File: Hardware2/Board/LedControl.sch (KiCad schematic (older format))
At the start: 49 parts, among them J2 Jumper, J3 Jumper, P1 USB_OTG, P10 TP, P11 2059-302, P12 DISPLAY, P13 TP, P14 Conn_01x03, P15 TP, P16 2059-302, P17 2059-302, P18 CONN_01X03, P19 CONN_01X03, P2 TP, P3 TP, P32 TP, P33 TP, P34 TP, P4 TP, P5 2059-302, P6 TP, P7 TP, P8 Micro_SD, P9 TP, SW1 PEC12R-4215F-S0024, SW2 PEC12R-4215F-S0024, U1 STM32L433CCUx, U2 SP485CN, U3 SP485CN, U4 SP485CN, X1 IQXO/7X

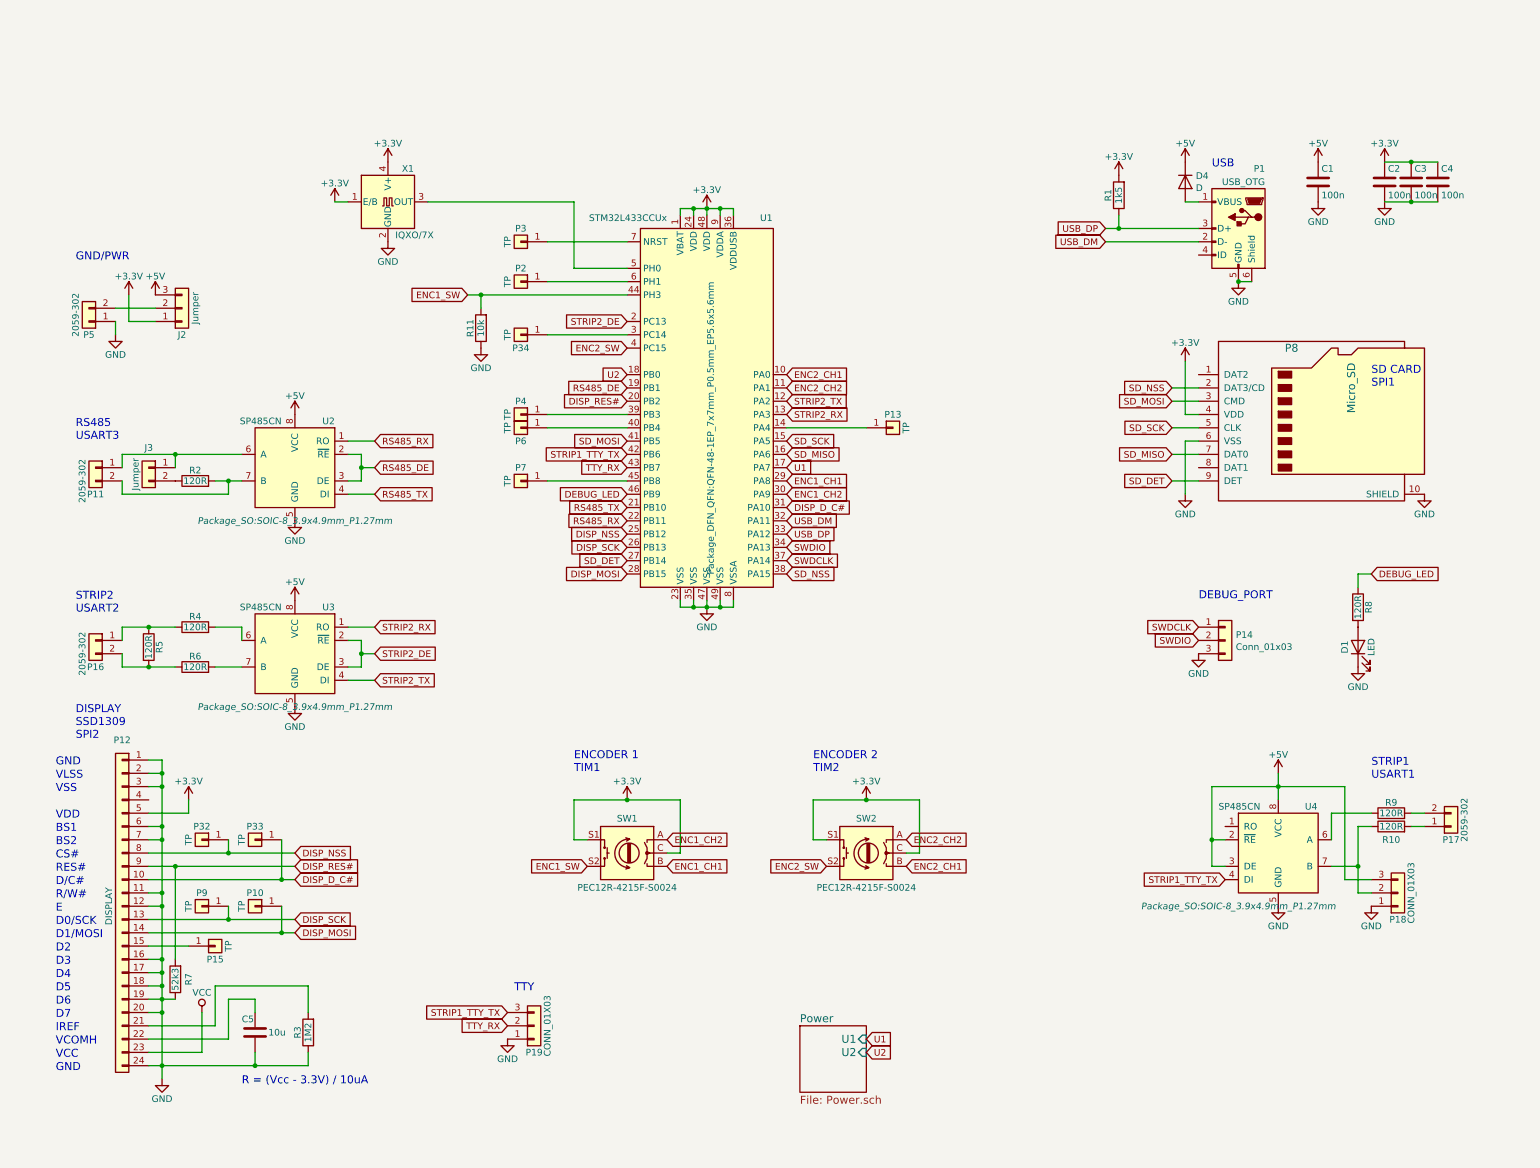
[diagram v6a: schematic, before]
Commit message: LED strip power supply below strip
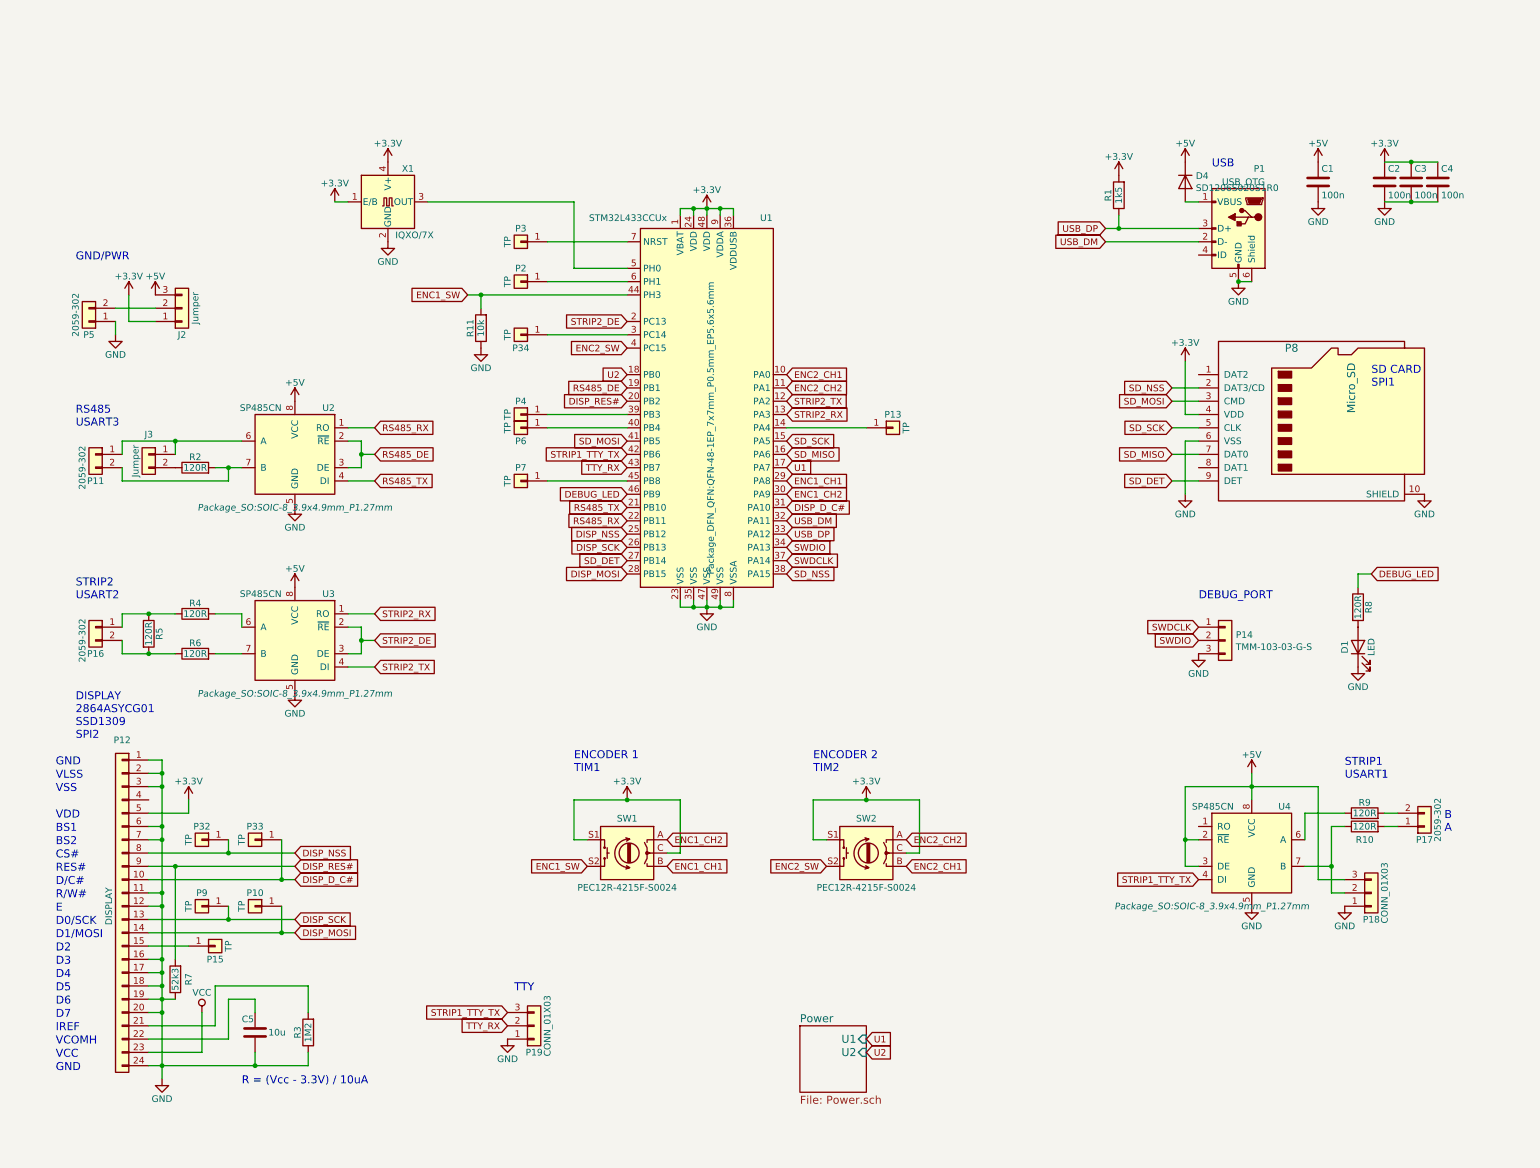
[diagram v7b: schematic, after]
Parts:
- D4: value D -> SD1206S020S1R0
- P14: value Conn_01x03 -> TMM-103-03-G-S
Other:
- note added: "B\nA"
- note added: "DISPLAY\n2864ASYCG01\nSSD1309\nSPI2"
- note removed: "DISPLAY\nSSD1309\nSPI2"
- moved on the sheet: J3, P11, P16, P17, P18, R10, R2, R4, R5, R6, R9, U2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

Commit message: Add CAN bus
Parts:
- removed J3: Jumper, LedControl:Jumper, symbol Connector_Generic:Conn_01x02
- removed P19: CONN_01X03, Connector_PinHeader_2.54mm:PinHeader_1x03_P2.54mm_Vertical, symbol Connector_Generic:Conn_01x03
- removed P3: TP, LedControl:Pad, symbol Connector_Generic:Conn_01x01
- removed U3: SP485CN, Package_SO:SOIC-8_3.9x4.9mm_P1.27mm, symbol Interface_UART:SP3485CN
- added C15, C16, C17: 100n, Capacitor_SMD:C_0603_1608Metric, symbol Device:C
- added D5, D6: SD1206S020S1R0, Diode_SMD:D_1206_3216Metric, symbol Device:D
- added J2: Jumper, LedControl:Jumper, symbol Connector_Generic:Conn_01x02
- added J3, J5: Jumper, LedControl:Jumper3, symbol Connector_Generic:Conn_01x04
- added P11: Header, Connector_PinHeader_2.54mm:PinHeader_1x04_P2.54mm_Vertical, symbol Connector_Generic:Conn_01x04
- added P17, P2, P4, P6, P9: 2059-302, LedControl:WAGO_2059-302, symbol Connector_Generic:Conn_01x02
- added P41, P42, P43, P44: TP, LedControl:Pad, symbol Connector_Generic:Conn_01x01
- added Q1, Q2: DMG1012UW, Package_TO_SOT_SMD:SOT-323_SC-70, symbol Transistor_FET:BSS214NW
- added R23, R24, R26, R28: 120R, Resistor_SMD:R_1206_3216Metric, symbol Device:R
- added R25, R27, R29, R8: 10k, Resistor_SMD:R_0603_1608Metric, symbol Device:R
- added U10: SP485CN, Package_SO:SOIC-8_3.9x4.9mm_P1.27mm, symbol Interface_UART:SP3485CN
- added U2: SN65HVD230, Package_SO:SOIC-8_3.9x4.9mm_P1.27mm, symbol Interface_CAN_LIN:SN65HVD230
- J4: renamed from J2; symbol Connector_Generic:Conn_01x03 -> Connector_Generic:Conn_01x04
- R22: renamed from R8; value 120R -> 390R; footprint Resistor_SMD:R_1206_3216Metric -> Resistor_SMD:R_0603_1608Metric
- R4, R6: value 120R -> 390R; footprint Resistor_SMD:R_1206_3216Metric -> Resistor_SMD:R_0603_1608Metric
- renumbered P8 to P10, P2 to P16, P7 to P19, P16 to P3, P4 to P36, P9 to P38, P6 to P39, P10 to P40, P11 to P7, P17 to P8, U2 to U3
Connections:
- net STRIP2_DE is gone; now on an unnamed net: U1.2 (PC13)
- net STRIP2_RX is gone; now on an unnamed net: U1.13 (PA3)
- net +3V3: now also J4.2 (Pin_2), SW1.S2, C15.1, J3.2 (Pin_2), J5.2 (Pin_2), R29.2, U2.3 (VCC); no longer J4.1 (Pin_1), SW1.S1
- net +5V: now also R4.1, C16.1, C17.1, D5.1 (K), D6.1 (K), J3.3 (Pin_3), J5.3 (Pin_3), R25.1, R27.1, U10.2 (~RE~), U10.3 (DE), U10.8 (VCC)
- net DEBUG_LED: now also U1.14 (PA4); no longer U1.46 (PB9)
- net DISP_RES#: now also P44.1 (Pin_1)
- net ENC1_CH1: now also SW1.A; no longer SW1.B
- net ENC1_CH2: now also SW1.B; no longer SW1.A
- net ENC1_SW: now also SW1.S1; no longer SW1.S2
- net ENC2_CH1: now also SW2.A; no longer SW2.B
- net ENC2_CH2: now also SW2.B; no longer SW2.A
- net GND: now also J4.4 (Pin_4), P14.1 (Pin_1), P7.2 (Pin_2), R6.2, C15.2, J2.1 (Pin_1), J3.4 (Pin_4), J5.4 (Pin_4), P11.1 (Pin_1), P17.2 (Pin_2), P4.1 (Pin_1), P43.1 (Pin_1), Q1.2 (S), Q2.2 (S), R8.2, U10.5 (GND), U2.2 (GND); no longer P14.3 (Pin_3)
- net RS485_RX: now also C17.2, R28.1
- net RS485_TX: now also C16.2, R26.1
- net STRIP1_TTY_TX: now also P41.1 (Pin_1)
- net STRIP2_TX: now also Q1.1 (G), U10.4 (DI)
- net SWDIO: now also P11.2 (Pin_2)
- net TTY_RX: now also P42.1 (Pin_1)
- net STRIP1_A: now reaches R10.2
- net STRIP1_A: now also P8.2 (Pin_2); no longer P8.1 (Pin_1)
- net STRIP1_B: now reaches R9.2
- net STRIP1_B: now also P8.1 (Pin_1); no longer P8.2 (Pin_2)
- net RS485A: now reaches R4.2
- net RS485A: now also R5.1, U3.6 (A), P6.1 (Pin_1), R25.2, R26.2
- net NRST: now reaches U1.7 (NRST)
- net NRST: now also P11.4 (Pin_4), R29.1
- net at P13.1 (Pin_1): now also Q2.1 (G); no longer U1.14 (PA4)
- net RS485B: now reaches R5.2, R6.1
- net RS485B: now also U3.7 (B), P6.2 (Pin_2), R27.2, R28.2; no longer P3.2 (Pin_2)
- net at P5.2 (Pin_2): now also J3.1 (Pin_1), P4.2 (Pin_2); no longer J4.2 (Pin_2)
- net at P19.1 (Pin_1): no longer U1.45 (PB8)
- net at P7.1 (Pin_1): now also J4.1 (Pin_1); no longer U3.6 (A)
- net CANH: now reaches R2.1
- net CANH: now also P3.2 (Pin_2), P2.2 (Pin_2), U2.7 (CANH)
- net SWDCLK renamed SWCLK
- net SWCLK: now also P14.3 (Pin_3), P11.3 (Pin_3); no longer P14.1 (Pin_1)
- new net: R23.1, U10.6 (A)
- new net: R24.1, U10.7 (B)
- new net: J5.1 (Pin_1), P17.1 (Pin_1)
- new net: J2.2 (Pin_2), R8.1, U2.8 (Rs)
- new net CANL: P2.1 (Pin_1), P3.1 (Pin_1), R2.2, U2.6 (CANL)
- new net CAN_RX: U1.45 (PB8), U2.4 (R)
- new net CAN_TX: U1.46 (PB9), U2.1 (D)
- new net STRIP2_A: D5.2 (A), P9.1 (Pin_1), Q1.3 (D), R24.2
- new net STRIP2_B: D6.2 (A), P9.2 (Pin_2), Q2.3 (D), R23.2
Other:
- note added: "Alternative to RS485"
- note added: "Alternative to STRIP2"
- note added: "BOOT0"
- note added: "CAN\nCAN1"
- note added: "DISPLAY\n2864ASYCG01 (SSD1309)\nSPI2"
- note added: "R3 = (Vcc - 3.3V) / 10uA"
- note added: "SWITCH INPUT"
- note added: "SWITCH OUTPUT"
- note removed: "DISPLAY\n2864ASYCG01\nSSD1309\nSPI2"
- note removed: "GND/PWR"
- note removed: "R = (Vcc - 3.3V) / 10uA"
- moved on the sheet: C1, C2, C3, C4, D1, D4, P1, P10, P13, P14, P16, P18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
